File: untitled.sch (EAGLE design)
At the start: 8 parts

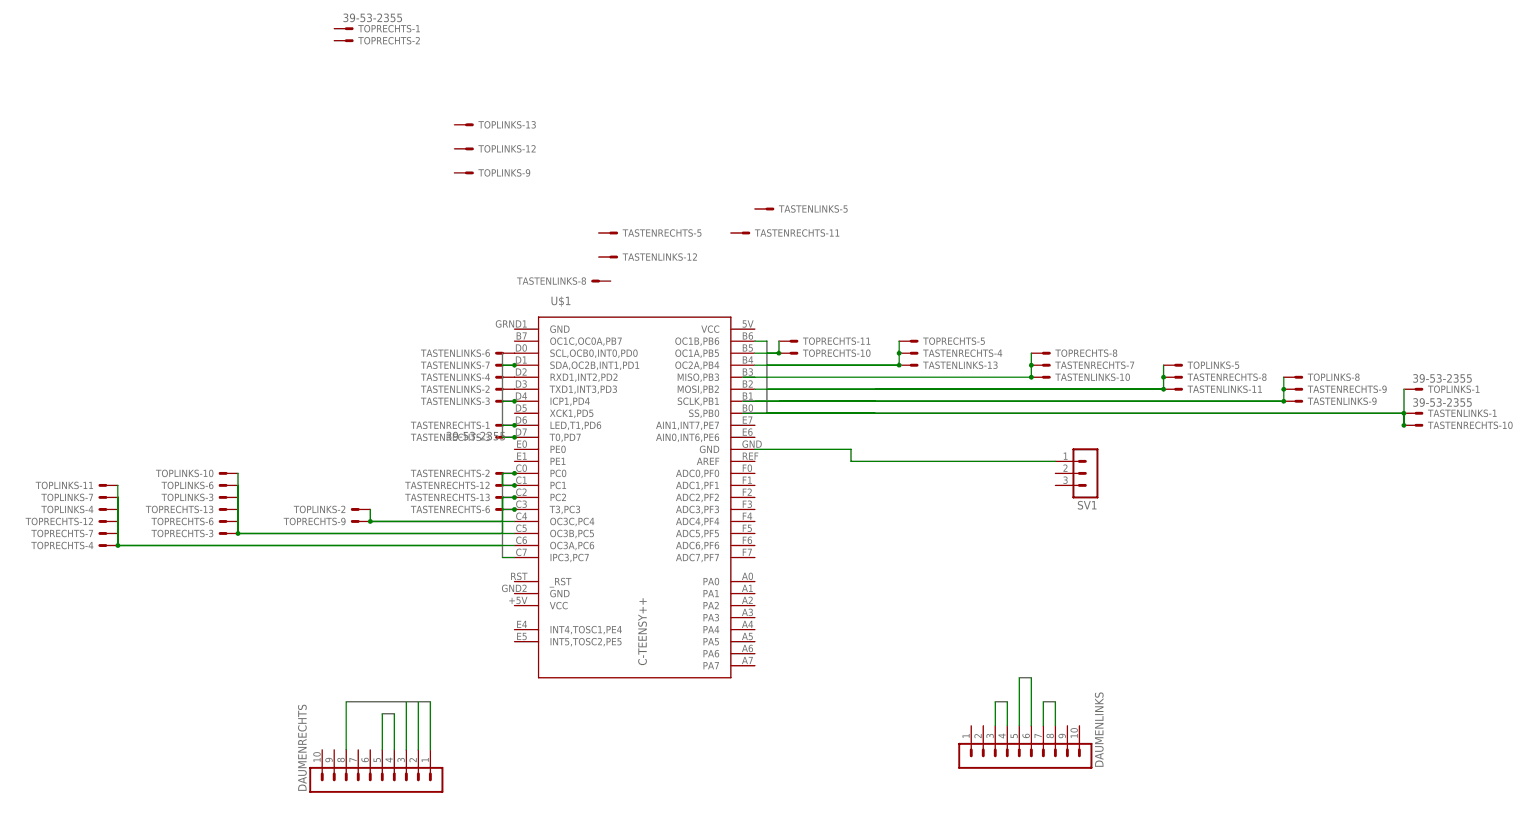
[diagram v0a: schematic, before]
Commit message: first autorouted version
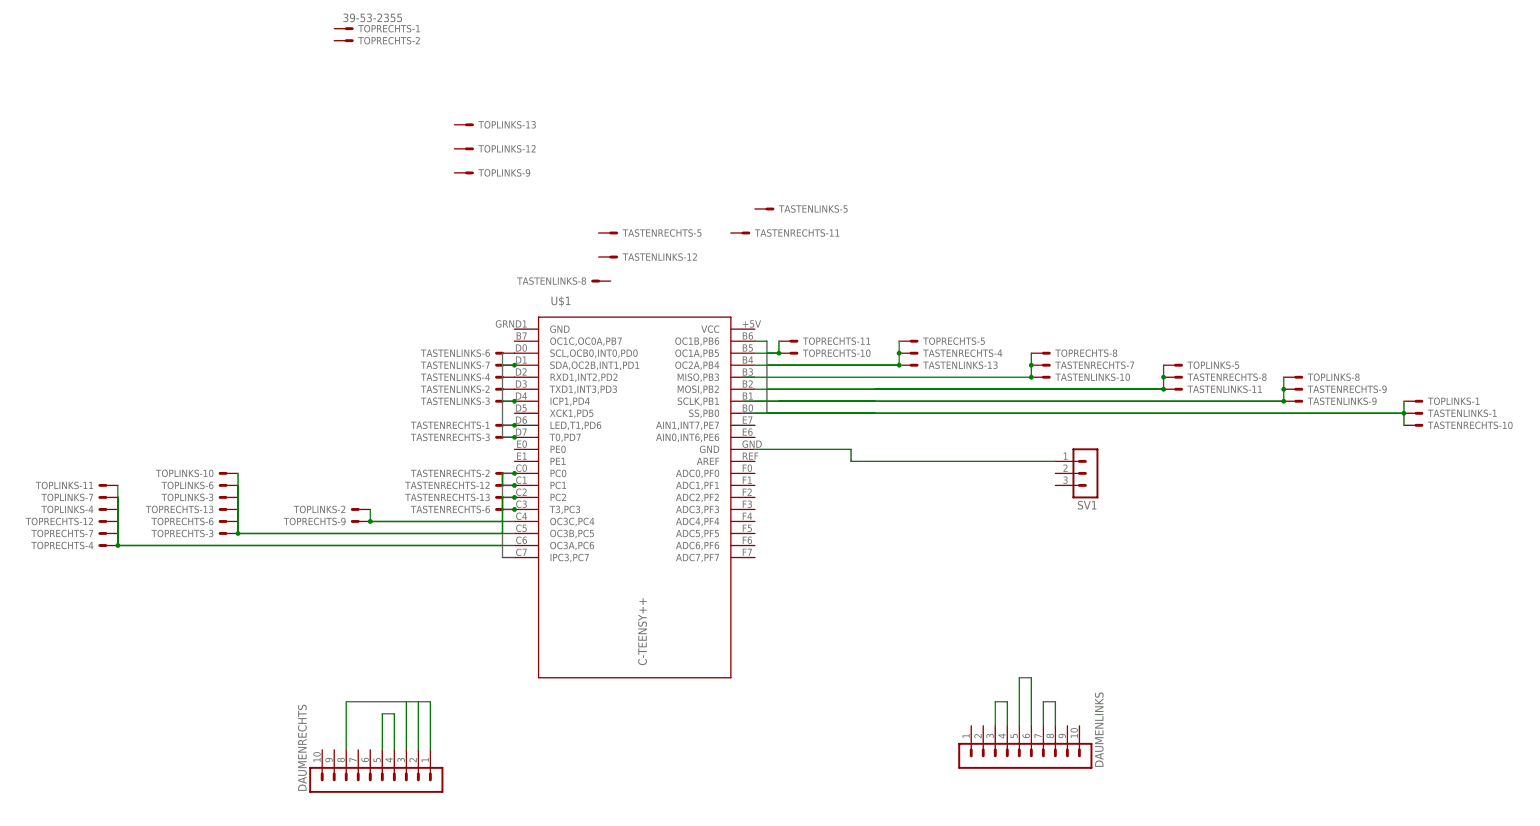
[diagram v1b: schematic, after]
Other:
- moved on the sheet: TOPLINKS-1
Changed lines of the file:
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@@
 <?xml version="1.0" encoding="utf-8"?>
 <!DOCTYPE eagle SYSTEM "eagle.dtd">
-<eagle version="6.3">
+<eagle version="6.4">
 <drawing>
 <settings>
@@
 <setting verticaltext="up"/>
 </settings>
-<grid distance="0.1" unitdist="inch" unit="inch" style="lines" multiple="1" display="no" altdistance="0.01" altunitdist="inch" altunit="inch"/>
+<grid distance="0.1" unitdist="inch" unit="inch" style="lines" multiple="1" display="yes" altdistance="0.01" altunitdist="inch" altunit="inch"/>
 <layers>
-<layer number="1" name="Top" color="4" fill="1" visible="no" active="no"/>
-<layer number="2" name="Route2" color="1" fill="3" visible="no" active="no"/>
-<layer number="3" name="Route3" color="4" fill="3" visible="no" active="no"/>
-<layer number="4" name="Route4" color="1" fill="4" visible="no" active="no"/>
-<layer number="5" name="Route5" color="4" fill="4" visible="no" active="no"/>
-<layer number="6" name="Route6" color="1" fill="8" visible="no" active="no"/>
-<layer number="7" name="Route7" color="4" fill="8" visible="no" active="no"/>
-<layer number="8" name="Route8" color="1" fill="2" visible="no" active="no"/>
-<layer number="9" name="Route9" color="4" fill="2" visible="no" active="no"/>
-<layer number="10" name="Route10" color="1" fill="7" visible="no" active="no"/>
-<layer number="11" name="Route11" color="4" fill="7" visible="no" active="no"/>
-<layer number="12" name="Route12" color="1" fill="5" visible="no" active="no"/>
-<layer number="13" name="Route13" color="4" fill="5" visible="no" active="no"/>
-<layer number="14" name="Route14" color="1" fill="6" visible="no" active="no"/>
-<layer number="15" name="Route15" color="4" fill="6" visible="no" active="no"/>
-<layer number="16" name="Bottom" color="1" fill="1" visible="no" active="no"/>
-<layer number="17" name="Pads" color="2" fill="1" visible="no" active="no"/>
-<layer number="18" name="Vias" color="2" fill="1" visible="no" active="no"/>
-<layer number="19" name="Unrouted" color="6" fill="1" visible="no" active="no"/>
-<layer number="20" name="Dimension" color="15" fill="1" visible="no" active="no"/>
-<layer number="21" name="tPlace" color="7" fill="1" visible="no" active="no"/>
-<layer number="22" name="bPlace" color="7" fill="1" visible="no" active="no"/>
-<layer number="23" name="tOrigins" color="15" fill="1" visible="no" active="no"/>
-<layer number="24" name="bOrigins" color="15" fill="1" visible="no" active="no"/>
-<layer number="25" name="tNames" color="7" fill="1" visible="no" active="no"/>
-<layer number="26" name="bNames" color="7" fill="1" visible="no" active="no"/>
-<layer number="27" name="tValues" color="7" fill="1" visible="no" active="no"/>
-<layer number="28" name="bValues" color="7" fill="1" visible="no" active="no"/>
+<layer number="1" name="Top" color="4" fill="1" visible="yes" active="no"/>
+<layer number="2" name="Route2" color="1" fill="3" visible="yes" active="no"/>
+<layer number="3" name="Route3" color="4" fill="3" visible="yes" active="no"/>
+<layer number="4" name="Route4" color="1" fill="4" visible="yes" active="no"/>
+<layer number="5" name="Route5" color="4" fill="4" visible="yes" active="no"/>
+<layer number="6" name="Route6" color="1" fill="8" visible="yes" active="no"/>
+<layer number="7" name="Route7" color="4" fill="8" visible="yes" active="no"/>
+<layer number="8" name="Route8" color="1" fill="2" visible="yes" active="no"/>
+<layer number="9" name="Route9" color="4" fill="2" visible="yes" active="no"/>
+<layer number="10" name="Route10" color="1" fill="7" visible="yes" active="no"/>
+<layer number="11" name="Route11" color="4" fill="7" visible="yes" active="no"/>
+<layer number="12" name="Route12" color="1" fill="5" visible="yes" active="no"/>
+<layer number="13" name="Route13" color="4" fill="5" visible="yes" active="no"/>
+<layer number="14" name="Route14" color="1" fill="6" visible="yes" active="no"/>
+<layer number="15" name="Route15" color="4" fill="6" visible="yes" active="no"/>
+<layer number="16" name="Bottom" color="1" fill="1" visible="yes" active="no"/>
+<layer number="17" name="Pads" color="2" fill="1" visible="yes" active="no"/>
+<layer number="18" name="Vias" color="2" fill="1" visible="yes" active="no"/>
+<layer number="19" name="Unrouted" color="6" fill="1" visible="yes" active="no"/>
+<layer number="20" name="Dimension" color="15" fill="1" visible="yes" active="no"/>
+<layer number="21" name="tPlace" color="7" fill="1" visible="yes" active="no"/>
+<layer number="22" name="bPlace" color="7" fill="1" visible="yes" active="no"/>
+<layer number="23" name="tOrigins" color="15" fill="1" visible="yes" active="no"/>
+<layer number="24" name="bOrigins" color="15" fill="1" visible="yes" active="no"/>
+<layer number="25" name="tNames" color="7" fill="1" visible="yes" active="no"/>
+<layer number="26" name="bNames" color="7" fill="1" visible="yes" active="no"/>
+<layer number="27" name="tValues" color="7" fill="1" visible="yes" active="no"/>
+<layer number="28" name="bValues" color="7" fill="1" visible="yes" active="no"/>
 <layer number="29" name="tStop" color="7" fill="3" visible="no" active="no"/>
 <layer number="30" name="bStop" color="7" fill="6" visible="no" active="no"/>
@@
 <layer number="35" name="tGlue" color="7" fill="4" visible="no" active="no"/>
 <layer number="36" name="bGlue" color="7" fill="5" visible="no" active="no"/>
-<layer number="37" name="tTest" color="7" fill="1" visible="no" active="no"/>
-<layer number="38" name="bTest" color="7" fill="1" visible="no" active="no"/>
+<layer number="37" name="tTest" color="7" fill="1" visible="yes" active="no"/>
+<layer number="38" name="bTest" color="7" fill="1" visible="yes" active="no"/>
 <layer number="39" name="tKeepout" color="4" fill="11" visible="no" active="no"/>
 <layer number="40" name="bKeepout" color="1" fill="11" visible="no" active="no"/>
@@
 <layer number="44" name="Drills" color="7" fill="1" visible="no" active="no"/>
 <layer number="45" name="Holes" color="7" fill="1" visible="no" active="no"/>
-<layer number="46" name="Milling" color="3" fill="1" visible="no" active="no"/>
-<layer number="47" name="Measures" color="7" fill="1" visible="no" active="no"/>
-<layer number="48" name="Document" color="7" fill="1" visible="no" active="no"/>
-<layer number="49" name="Reference" color="7" fill="1" visible="no" active="no"/>
-<layer number="51" name="tDocu" color="7" fill="1" visible="no" active="no"/>
-<layer number="52" name="bDocu" color="7" fill="1" visible="no" active="no"/>
+<layer number="46" name="Milling" color="3" fill="1" visible="yes" active="no"/>
+<layer number="47" name="Measures" color="7" fill="1" visible="yes" active="no"/>
+<layer number="48" name="Document" color="7" fill="1" visible="yes" active="no"/>
+<layer number="49" name="Reference" color="7" fill="1" visible="yes" active="no"/>
+<layer number="51" name="tDocu" color="7" fill="1" visible="yes" active="no"/>
+<layer number="52" name="bDocu" color="7" fill="1" visible="yes" active="no"/>
 <layer number="91" name="Nets" color="2" fill="1" visible="yes" active="yes"/>
 <layer number="92" name="Busses" color="1" fill="1" visible="yes" active="yes"/>
@@
 <instance part="TASTENRECHTS" gate="-12" x="38.1" y="40.64" rot="R180"/>
 <instance part="TASTENRECHTS" gate="-13" x="38.1" y="38.1" rot="R180"/>
-<instance part="TASTENRECHTS" gate="-1" x="40.64" y="53.34" rot="R180"/>
+<instance part="TASTENRECHTS" gate="-1" x="40.64" y="53.34" smashed="yes" rot="R180">
+<attribute name="NAME" x="35.56" y="54.102" size="1.524" layer="95" rot="R180"/>
+</instance>
 <instance part="TOPRECHTS" gate="-2" x="5.08" y="134.62"/>
 <instance part="TOPRECHTS" gate="-3" x="-20.32" y="30.48" rot="R180"/>
@@
 <instance part="TOPLINKS" gate="-12" x="30.48" y="111.76"/>
 <instance part="TOPLINKS" gate="-13" x="30.48" y="116.84"/>
-<instance part="TOPLINKS" gate="-1" x="228.6" y="60.96"/>
+<instance part="TOPLINKS" gate="-1" x="228.6" y="58.42" smashed="yes">
+<attribute name="NAME" x="233.68" y="57.658" size="1.524" layer="95"/>
+</instance>
 <instance part="TASTENLINKS" gate="-2" x="38.1" y="60.96" rot="R180"/>
 <instance part="TASTENLINKS" gate="-3" x="38.1" y="58.42" rot="R180"/>
@@
 <instance part="TASTENLINKS" gate="-12" x="60.96" y="88.9"/>
 <instance part="TASTENLINKS" gate="-13" x="124.46" y="66.04"/>
-<instance part="TASTENLINKS" gate="-1" x="228.6" y="55.88"/>
+<instance part="TASTENLINKS" gate="-1" x="228.6" y="55.88" smashed="yes">
+<attribute name="NAME" x="233.68" y="55.118" size="1.524" layer="95"/>
+</instance>
 </instances>
 <busses>
@@
 <junction x="228.6" y="55.88"/>
 <pinref part="TOPLINKS" gate="-1" pin="S"/>
-<wire x1="228.6" y1="60.96" x2="228.6" y2="53.34" width="0.1524" layer="91"/>
+<wire x1="228.6" y1="58.42" x2="228.6" y2="55.88" width="0.1524" layer="91"/>
 <wire x1="228.6" y1="53.34" x2="228.6" y2="55.88" width="0.1524" layer="91"/>
 <wire x1="228.6" y1="55.88" x2="91.44" y2="55.88" width="0.1524" layer="91"/>
 <pinref part="TASTENRECHTS" gate="-10" pin="S"/>
-<junction x="228.6" y="53.34"/>
-</segment>
-</net>
+</segment>
+</net>

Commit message: fixed wiring
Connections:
- net D1 renamed N$1
- net N$14 renamed GND
- removed net C7: U$1.IPC3,PC7
- removed net N$16: TASTENLINKS-2.S, U$1.TXD1,INT3,PD3
- removed net N$17: TASTENLINKS-4.S, U$1.RXD1,INT2,PD2
- net D2: now also TASTENLINKS-4.S, U$1.RXD1,INT2,PD2
- net D3: now also TASTENLINKS-2.S, U$1.TXD1,INT3,PD3
- net D5: now also U$1.XCK1,PD5
- net N$2: now also U$1.MISO,PB3
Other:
- moved on the sheet: DAUMENLINKS, DAUMENRECHTS, SV1, TASTENLINKS-1, TASTENLINKS-11, TASTENLINKS-2, TASTENLINKS-3, TASTENLINKS-4, TASTENLINKS-6, TASTENLINKS-7, TASTENLINKS-9, TASTENRECHTS-1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

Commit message: renamed nets to pinout
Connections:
- net N$1 renamed D1
- net N$18 renamed D0
- net N$2 renamed B3
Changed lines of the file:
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@@
 </segment>
 </net>
-<net name="N$2" class="0">
+<net name="B3" class="0">
 <segment>
 <pinref part="TOPRECHTS" gate="-8" pin="S"/>
@@
 </segment>
 </net>
-<net name="N$18" class="0">
+<net name="D0" class="0">
 <segment>
 <pinref part="U$1" gate="G$1" pin="SCL,OCB0,INT0,PD0"/>
@@
 </segment>
 </net>
-<net name="N$1" class="0">
+<net name="D1" class="0">
 <segment>
 <pinref part="TASTENLINKS" gate="-7" pin="S"/>

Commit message: half-optimized
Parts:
- removed SV1: (no value), con-lstb:MA03-1
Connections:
- removed net GND: SV1.1, U$1.GND@1
- new net N$1: U$1.GND@1
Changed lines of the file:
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@@
 <part name="DAUMENLINKS" library="con-lstb" deviceset="MA10-1" device=""/>
 <part name="U$1" library="teensypp" deviceset="C-TEENSY++" device=""/>
-<part name="SV1" library="con-lstb" deviceset="MA03-1" device=""/>
 <part name="TASTENRECHTS" library="con-molex-39-53" deviceset="39-53-2355" device=""/>
 <part name="TOPRECHTS" library="con-molex-39-53" deviceset="39-53-2355" device=""/>
@@
 <instance part="DAUMENLINKS" gate="1" x="109.22" y="-27.94" rot="MR90"/>
 <instance part="U$1" gate="G$1" x="66.04" y="45.72"/>
-<instance part="SV1" gate="G$1" x="109.22" y="45.72" rot="R180"/>
 <instance part="TASTENRECHTS" gate="-2" x="12.7" y="43.18" rot="R180"/>
 <instance part="TASTENRECHTS" gate="-3" x="12.7" y="50.8" rot="R180"/>
@@
 </segment>
 </net>
-<net name="GND" class="0">
+<net name="N$1" class="0">
 <segment>
 <pinref part="U$1" gate="G$1" pin="GND@1"/>
-<pinref part="SV1" gate="G$1" pin="1"/>
-<wire x1="91.44" y1="48.26" x2="101.6" y2="48.26" width="0.1524" layer="91"/>
-</segment>
-</net>
+<wire x1="91.44" y1="48.26" x2="96.52" y2="48.26" width="0.1524" layer="91"/>
+</segment>
+</net>

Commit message: Layout fertiggestellt fürs PCB
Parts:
- added LED1, LED2, LED3, LED4: (no value), led:LED3MM
- added R1, R2, R3, R4: (no value), rcl:R-EU_R1206
- renumbered U$1 to U1
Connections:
- new net N$10: R4.2, U1.ADC0,PF0
- new net N$11: LED1.A, LED2.A, LED3.A, LED4.A, U1.VCC
- new net N$14: LED4.C, R4.1
- new net N$15: LED3.C, R3.1
- new net N$16: LED2.C, R2.1
- new net N$17: LED1.C, R1.1
- new net N$7: R1.2, U1.ADC3,PF3
- new net N$8: R2.2, U1.ADC2,PF2
- new net N$9: R3.2, U1.ADC1,PF1
- net B3: now also TASTENLINKS-12.S; no longer TASTENLINKS-10.S
- net D0: now also TASTENLINKS-8.S; no longer TASTENLINKS-6.S
- net D2: now also TASTENLINKS-6.S; no longer TASTENLINKS-4.S
- net D3: now also TASTENLINKS-4.S; no longer TASTENLINKS-2.S
- net D5: now also TASTENLINKS-2.S
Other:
- moved on the sheet: TASTENLINKS-10, TASTENLINKS-12, TASTENLINKS-2, TASTENLINKS-4, TASTENLINKS-6, TASTENLINKS-8
